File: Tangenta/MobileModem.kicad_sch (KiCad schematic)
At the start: 12 parts, among them J18 1-2199230-5, J19 HYC90-SIM06-180

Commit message: Schematic improvements.
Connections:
- net VPP: no longer names the net of J19.5 (VPP)
- no-connect marks 45 -> 47
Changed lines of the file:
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@@
   (no_connect (at 86.36 123.19))
   (no_connect (at 86.36 113.03))
+  (no_connect (at 39.37 170.18))
   (no_connect (at 60.96 72.39))
   (no_connect (at 151.13 95.25))
   (no_connect (at 60.96 74.93))
   (no_connect (at 60.96 52.07))
+  (no_connect (at 158.75 87.63))
   (no_connect (at 147.32 95.25))
   (no_connect (at 86.36 102.87))
@@
     (stroke (width 0) (type default))
   )
-  (wire (pts (xy 158.75 87.63) (xy 170.18 87.63))
-    (stroke (width 0) (type default))
-  )
   (wire (pts (xy 60.96 100.33) (xy 44.45 100.33))
     (stroke (width 0) (type default))
@@
     (effects (font (size 1.27 1.27)) (justify left bottom))
   )
-  (label "VPP" (at 170.18 87.63 180) (fields_autoplaced)
-    (effects (font (size 1.27 1.27)) (justify right bottom))
-  )
   (label "UIM1_CLK" (at 106.68 90.17 0) (fields_autoplaced)

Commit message: Libraries exported from global to project.
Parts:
- C1: symbol Device:C_Small -> CholaSymbolsPrjLib:C_Small
- H10, H11: symbol Mechanical:MountingHole -> CholaSymbolsPrjLib:MountingHole
- J18: symbol M2_Slot:1-2199230-5 -> CholaSymbolsPrjLib:1-2199230-5
- J19: symbol SIM_Holder:HYC90-SIM06-180 -> CholaSymbolsPrjLib:HYC90-SIM06-180
- R2: symbol Device:R_Small_US -> CholaSymbolsPrjLib:R_Small_US
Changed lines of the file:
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@@
     (effects (font (size 1.27 1.27)) (justify right))
   )
-  (symbol (lib_id "SIM_Holder:HYC90-SIM06-180") (at 148.59 87.63 0) (unit 1)
+  (symbol (lib_id "CholaSymbolsPrjLib:HYC90-SIM06-180") (at 148.59 87.63 0) (unit 1)
     (in_bom yes) (on_board yes) (dnp no) (fields_autoplaced)
     (property "Reference" "J19" (at 148.59 78.74 0)
@@
     )
   )
-  (symbol (lib_id "Mechanical:MountingHole") (at 186.055 76.2 0) (unit 1)
+  (symbol (lib_id "CholaSymbolsPrjLib:MountingHole") (at 186.055 76.2 0) (unit 1)
     (in_bom yes) (on_board yes) (dnp no)
     (property "Reference" "H10" (at 188.595 76.2 0)
@@
     )
   )
-  (symbol (lib_id "Device:C_Small") (at 140.97 68.58 180) (unit 1)
+  (symbol (lib_id "CholaSymbolsPrjLib:C_Small") (at 140.97 68.58 180) (unit 1)
     (in_bom yes) (on_board yes) (dnp no)
     (property "Reference" "C1" (at 137.16 68.58 0)
@@
     )
   )
-  (symbol (lib_id "Device:C_Small") (at 156.21 68.58 180) (unit 1)
+  (symbol (lib_id "CholaSymbolsPrjLib:C_Small") (at 156.21 68.58 180) (unit 1)
     (in_bom yes) (on_board yes) (dnp no)
     (property "Reference" "C1" (at 160.02 68.58 0)
@@
     )
   )
-  (symbol (lib_id "Device:R_Small_US") (at 173.99 74.93 180) (unit 1)
+  (symbol (lib_id "CholaSymbolsPrjLib:R_Small_US") (at 173.99 74.93 180) (unit 1)
     (in_bom yes) (on_board yes) (dnp no)
     (property "Reference" "R2" (at 172.72 74.93 0)
@@
     )
   )
-  (symbol (lib_id "Device:R_Small_US") (at 54.61 77.47 90) (unit 1)
+  (symbol (lib_id "CholaSymbolsPrjLib:R_Small_US") (at 54.61 77.47 90) (unit 1)
     (in_bom yes) (on_board yes) (dnp no)
     (property "Reference" "R2" (at 53.34 76.2 90)
@@
     )
   )
-  (symbol (lib_id "Device:C_Small") (at 124.46 95.25 180) (unit 1)
+  (symbol (lib_id "CholaSymbolsPrjLib:C_Small") (at 124.46 95.25 180) (unit 1)
     (in_bom yes) (on_board yes) (dnp no)
     (property "Reference" "C1" (at 120.65 95.25 0)
@@
     )
   )
-  (symbol (lib_id "Mechanical:MountingHole") (at 186.055 83.82 0) (unit 1)
+  (symbol (lib_id "CholaSymbolsPrjLib:MountingHole") (at 186.055 83.82 0) (unit 1)
     (in_bom yes) (on_board yes) (dnp no)
     (property "Reference" "H11" (at 188.595 83.82 0)
@@
     )
   )
-  (symbol (lib_id "Device:R_Small_US") (at 92.71 57.15 270) (mirror x) (unit 1)
+  (symbol (lib_id "CholaSymbolsPrjLib:R_Small_US") (at 92.71 57.15 270) (mirror x) (unit 1)
     (in_bom yes) (on_board yes) (dnp no)
     (property "Reference" "R2" (at 87.63 55.88 90)
@@
     )
   )
-  (symbol (lib_id "Device:R_Small_US") (at 54.61 128.27 90) (unit 1)
+  (symbol (lib_id "CholaSymbolsPrjLib:R_Small_US") (at 54.61 128.27 90) (unit 1)
     (in_bom yes) (on_board yes) (dnp no)
     (property "Reference" "R2" (at 53.34 127 90)
@@
     )
   )
-  (symbol (lib_id "Device:R_Small_US") (at 124.46 104.14 180) (unit 1)
+  (symbol (lib_id "CholaSymbolsPrjLib:R_Small_US") (at 124.46 104.14 180) (unit 1)
     (in_bom yes) (on_board yes) (dnp no)
     (property "Reference" "R2" (at 123.19 104.14 0)
@@
     )
   )
-  (symbol (lib_id "M2_Slot:1-2199230-5") (at 73.66 44.45 90) (mirror x) (unit 1)
+  (symbol (lib_id "CholaSymbolsPrjLib:1-2199230-5") (at 73.66 44.45 90) (mirror x) (unit 1)
     (in_bom yes) (on_board yes) (dnp no)
     (property "Reference" "J18" (at 66.04 46.99 90)

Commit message: GND ready, before re-annotation.
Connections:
- net CHASSIS: no longer J18.MP1
- no-connect marks 47 -> 48
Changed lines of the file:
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@@
   (no_connect (at 86.36 107.95))
   (no_connect (at 60.96 125.73))
+  (no_connect (at 73.66 44.45))
   (no_connect (at 86.36 82.55))
   (no_connect (at 60.96 97.79))
@@
     (stroke (width 0) (type default))
   )
-  (wire (pts (xy 73.66 41.91) (xy 82.55 41.91))
-    (stroke (width 0) (type default))
-  )
   (wire (pts (xy 86.36 128.27) (xy 102.87 128.27))
     (stroke (width 0) (type default))
@@
     (stroke (width 0) (type default))
   )
-  (wire (pts (xy 73.66 41.91) (xy 73.66 44.45))
-    (stroke (width 0) (type default))
-  )
   (wire (pts (xy 148.59 72.39) (xy 156.21 72.39))
     (stroke (width 0) (type default))
@@
     (effects (font (size 1.27 1.27)) (justify right bottom))
   )
-  (label "CHASSIS" (at 82.55 41.91 180) (fields_autoplaced)
-    (effects (font (size 1.27 1.27)) (justify right bottom))
-  )

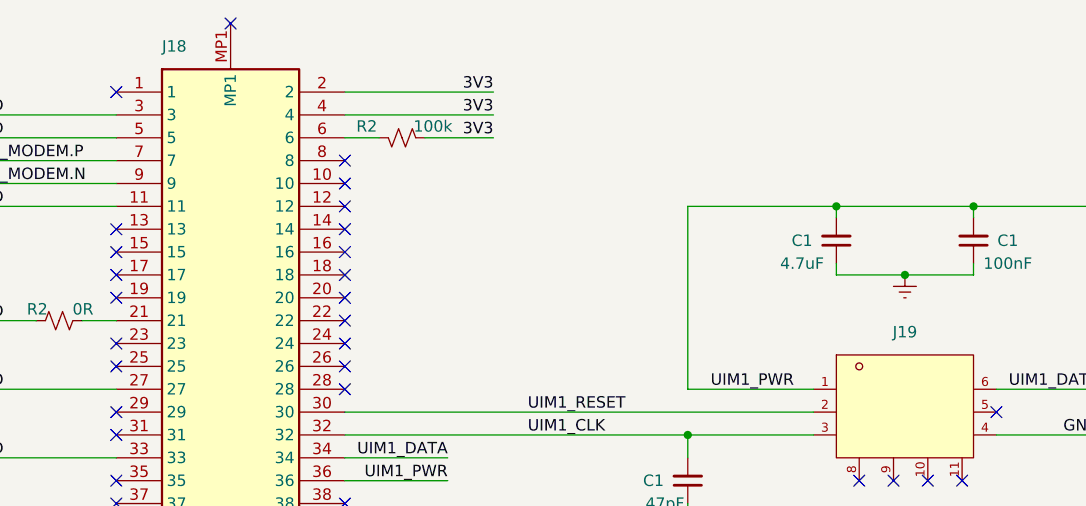
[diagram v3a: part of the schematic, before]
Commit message: Re-annotated. Ready for JLCPCB design verification.
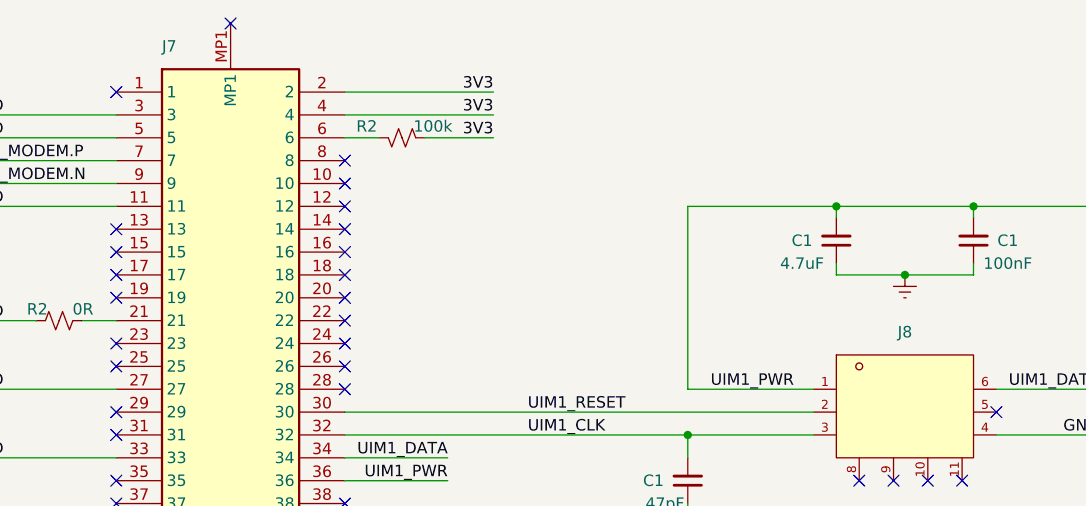
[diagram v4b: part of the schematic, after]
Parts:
- renumbered J18 to J7, J19 to J8
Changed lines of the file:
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@@
   (symbol (lib_id "CholaSymbolsPrjLib:HYC90-SIM06-180") (at 148.59 87.63 0) (unit 1)
     (in_bom yes) (on_board yes) (dnp no) (fields_autoplaced)
-    (property "Reference" "J19" (at 148.59 78.74 0)
+    (property "Reference" "J8" (at 148.59 78.74 0)
       (effects (font (size 1.27 1.27)))
     )
@@
       (project "Tangenta"
         (path "/358d1bcf-7599-4352-8c4d-baa18a5f09e6/f1c5822c-e7b8-40ae-bab0-71fd1c2cfc7c"
-          (reference "J19") (unit 1)
+          (reference "J8") (unit 1)
         )
       )
@@
         )
         (path "/358d1bcf-7599-4352-8c4d-baa18a5f09e6/f1c5822c-e7b8-40ae-bab0-71fd1c2cfc7c"
-          (reference "#PWR045") (unit 1)
+          (reference "#PWR050") (unit 1)
         )
       )
@@
         )
         (path "/358d1bcf-7599-4352-8c4d-baa18a5f09e6/f1c5822c-e7b8-40ae-bab0-71fd1c2cfc7c"
-          (reference "C85") (unit 1)
+          (reference "C71") (unit 1)
         )
       )
@@
         )
         (path "/358d1bcf-7599-4352-8c4d-baa18a5f09e6/f1c5822c-e7b8-40ae-bab0-71fd1c2cfc7c"
-          (reference "C86") (unit 1)
+          (reference "C72") (unit 1)
         )
       )
@@
         )
         (path "/358d1bcf-7599-4352-8c4d-baa18a5f09e6/f1c5822c-e7b8-40ae-bab0-71fd1c2cfc7c"
-          (reference "R52") (unit 1)
+          (reference "R46") (unit 1)
         )
       )
@@
         )
         (path "/358d1bcf-7599-4352-8c4d-baa18a5f09e6/f1c5822c-e7b8-40ae-bab0-71fd1c2cfc7c"
-          (reference "#PWR046") (unit 1)
+          (reference "#PWR051") (unit 1)
         )
       )
@@
         )
         (path "/358d1bcf-7599-4352-8c4d-baa18a5f09e6/f1c5822c-e7b8-40ae-bab0-71fd1c2cfc7c"
-          (reference "R48") (unit 1)
+          (reference "R42") (unit 1)
         )
       )
@@
         )
         (path "/358d1bcf-7599-4352-8c4d-baa18a5f09e6/f1c5822c-e7b8-40ae-bab0-71fd1c2cfc7c"
-          (reference "C84") (unit 1)
+          (reference "C70") (unit 1)
         )
       )
@@
         )
         (path "/358d1bcf-7599-4352-8c4d-baa18a5f09e6/f1c5822c-e7b8-40ae-bab0-71fd1c2cfc7c"
-          (reference "R50") (unit 1)
+          (reference "R44") (unit 1)
         )
       )
@@
         )
         (path "/358d1bcf-7599-4352-8c4d-baa18a5f09e6/f1c5822c-e7b8-40ae-bab0-71fd1c2cfc7c"
-          (reference "R49") (unit 1)
+          (reference "R43") (unit 1)
         )
       )
@@
         )
         (path "/358d1bcf-7599-4352-8c4d-baa18a5f09e6/f1c5822c-e7b8-40ae-bab0-71fd1c2cfc7c"
-          (reference "#PWR035") (unit 1)
+          (reference "#PWR049") (unit 1)
         )
       )
@@
         )
         (path "/358d1bcf-7599-4352-8c4d-baa18a5f09e6/f1c5822c-e7b8-40ae-bab0-71fd1c2cfc7c"
-          (reference "R51") (unit 1)
+          (reference "R45") (unit 1)
         )
       )
@@
   (symbol (lib_id "CholaSymbolsPrjLib:1-2199230-5") (at 73.66 44.45 90) (mirror x) (unit 1)
     (in_bom yes) (on_board yes) (dnp no)
-    (property "Reference" "J18" (at 66.04 46.99 90)
+    (property "Reference" "J7" (at 66.04 46.99 90)
       (effects (font (size 1.27 1.27)) (justify right))
     )
@@
       (project "Tangenta"
         (path "/358d1bcf-7599-4352-8c4d-baa18a5f09e6/f1c5822c-e7b8-40ae-bab0-71fd1c2cfc7c"
-          (reference "J18") (unit 1)
-        )
-      )
+          (reference "J7") (unit 1)
+        )
+      )

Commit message: initialize branch
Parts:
- renumbered C1 to C70, C1 to C71, C1 to C72, R2 to R42, R2 to R43, R2 to R44, R2 to R45, R2 to R46
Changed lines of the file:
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@@
   (symbol (lib_id "power:GNDREF") (at 124.46 111.76 0) (unit 1)
     (in_bom yes) (on_board yes) (dnp no) (fields_autoplaced)
-    (property "Reference" "#PWR030" (at 124.46 118.11 0)
+    (property "Reference" "#PWR050" (at 124.46 118.11 0)
       (effects (font (size 1.27 1.27)) hide)
     )
@@
     (instances
       (project "Tangenta"
-        (path "/358d1bcf-7599-4352-8c4d-baa18a5f09e6/b1871a4d-6a35-44e2-a9a2-9a4af684371d"
-          (reference "#PWR030") (unit 1)
-        )
         (path "/358d1bcf-7599-4352-8c4d-baa18a5f09e6/f1c5822c-e7b8-40ae-bab0-71fd1c2cfc7c"
           (reference "#PWR050") (unit 1)
@@
   (symbol (lib_id "CholaSymbolsPrjLib:C_Small") (at 140.97 68.58 180) (unit 1)
     (in_bom yes) (on_board yes) (dnp no)
-    (property "Reference" "C1" (at 137.16 68.58 0)
+    (property "Reference" "C71" (at 137.16 68.58 0)
       (effects (font (size 1.27 1.27)))
     )
@@
     (instances
       (project "Tangenta"
-        (path "/358d1bcf-7599-4352-8c4d-baa18a5f09e6/8215796b-9611-4f43-bcc5-319f8414b8a6"
-          (reference "C1") (unit 1)
-        )
-        (path "/358d1bcf-7599-4352-8c4d-baa18a5f09e6/d6c05402-162e-441f-bed8-be7996260fb4"
-          (reference "C9") (unit 1)
-        )
-        (path "/358d1bcf-7599-4352-8c4d-baa18a5f09e6/b1871a4d-6a35-44e2-a9a2-9a4af684371d"
-          (reference "C35") (unit 1)
-        )
         (path "/358d1bcf-7599-4352-8c4d-baa18a5f09e6/f1c5822c-e7b8-40ae-bab0-71fd1c2cfc7c"
           (reference "C71") (unit 1)
@@
   (symbol (lib_id "CholaSymbolsPrjLib:C_Small") (at 156.21 68.58 180) (unit 1)
     (in_bom yes) (on_board yes) (dnp no)
-    (property "Reference" "C1" (at 160.02 68.58 0)
+    (property "Reference" "C72" (at 160.02 68.58 0)
       (effects (font (size 1.27 1.27)))
     )
@@
     (instances
       (project "Tangenta"
-        (path "/358d1bcf-7599-4352-8c4d-baa18a5f09e6/8215796b-9611-4f43-bcc5-319f8414b8a6"
-          (reference "C1") (unit 1)
-        )
-        (path "/358d1bcf-7599-4352-8c4d-baa18a5f09e6/d6c05402-162e-441f-bed8-be7996260fb4"
-          (reference "C9") (unit 1)
-        )
-        (path "/358d1bcf-7599-4352-8c4d-baa18a5f09e6/b1871a4d-6a35-44e2-a9a2-9a4af684371d"
-          (reference "C35") (unit 1)
-        )
         (path "/358d1bcf-7599-4352-8c4d-baa18a5f09e6/f1c5822c-e7b8-40ae-bab0-71fd1c2cfc7c"
           (reference "C72") (unit 1)
@@
   (symbol (lib_id "CholaSymbolsPrjLib:R_Small_US") (at 173.99 74.93 180) (unit 1)
     (in_bom yes) (on_board yes) (dnp no)
-    (property "Reference" "R2" (at 172.72 74.93 0)
+    (property "Reference" "R46" (at 172.72 74.93 0)
       (effects (font (size 1.27 1.27)) (justify left))
     )
@@
     (instances
       (project "Tangenta"
-        (path "/358d1bcf-7599-4352-8c4d-baa18a5f09e6/8215796b-9611-4f43-bcc5-319f8414b8a6"
-          (reference "R2") (unit 1)
-        )
-        (path "/358d1bcf-7599-4352-8c4d-baa18a5f09e6/d6c05402-162e-441f-bed8-be7996260fb4"
-          (reference "R18") (unit 1)
-        )
-        (path "/358d1bcf-7599-4352-8c4d-baa18a5f09e6/b1871a4d-6a35-44e2-a9a2-9a4af684371d"
-          (reference "R26") (unit 1)
-        )
         (path "/358d1bcf-7599-4352-8c4d-baa18a5f09e6/f1c5822c-e7b8-40ae-bab0-71fd1c2cfc7c"
           (reference "R46") (unit 1)
@@
   (symbol (lib_id "power:GNDREF") (at 148.59 72.39 0) (unit 1)
     (in_bom yes) (on_board yes) (dnp no) (fields_autoplaced)
-    (property "Reference" "#PWR030" (at 148.59 78.74 0)
+    (property "Reference" "#PWR051" (at 148.59 78.74 0)
       (effects (font (size 1.27 1.27)) hide)
     )
@@
     (instances
       (project "Tangenta"
-        (path "/358d1bcf-7599-4352-8c4d-baa18a5f09e6/b1871a4d-6a35-44e2-a9a2-9a4af684371d"
-          (reference "#PWR030") (unit 1)
-        )
         (path "/358d1bcf-7599-4352-8c4d-baa18a5f09e6/f1c5822c-e7b8-40ae-bab0-71fd1c2cfc7c"
           (reference "#PWR051") (unit 1)
@@
   (symbol (lib_id "CholaSymbolsPrjLib:R_Small_US") (at 54.61 77.47 90) (unit 1)
     (in_bom yes) (on_board yes) (dnp no)
-    (property "Reference" "R2" (at 53.34 76.2 90)
+    (property "Reference" "R42" (at 53.34 76.2 90)
       (effects (font (size 1.27 1.27)) (justify left))
     )
@@
     (instances
       (project "Tangenta"
-        (path "/358d1bcf-7599-4352-8c4d-baa18a5f09e6/8215796b-9611-4f43-bcc5-319f8414b8a6"
-          (reference "R2") (unit 1)
-        )
-        (path "/358d1bcf-7599-4352-8c4d-baa18a5f09e6/d6c05402-162e-441f-bed8-be7996260fb4"
-          (reference "R18") (unit 1)
-        )
-        (path "/358d1bcf-7599-4352-8c4d-baa18a5f09e6/b1871a4d-6a35-44e2-a9a2-9a4af684371d"
-          (reference "R26") (unit 1)
-        )
-        (path "/358d1bcf-7599-4352-8c4d-baa18a5f09e6/6a8c68b5-4a7d-449e-86f6-34ced6d1cb55"
-          (reference "R45") (unit 1)
-        )
         (path "/358d1bcf-7599-4352-8c4d-baa18a5f09e6/f1c5822c-e7b8-40ae-bab0-71fd1c2cfc7c"
           (reference "R42") (unit 1)
@@
   (symbol (lib_id "CholaSymbolsPrjLib:C_Small") (at 124.46 95.25 180) (unit 1)
     (in_bom yes) (on_board yes) (dnp no)
-    (property "Reference" "C1" (at 120.65 95.25 0)
+    (property "Reference" "C70" (at 120.65 95.25 0)
       (effects (font (size 1.27 1.27)))
     )
@@
     (instances
       (project "Tangenta"
-        (path "/358d1bcf-7599-4352-8c4d-baa18a5f09e6/8215796b-9611-4f43-bcc5-319f8414b8a6"
-          (reference "C1") (unit 1)
-        )
-        (path "/358d1bcf-7599-4352-8c4d-baa18a5f09e6/d6c05402-162e-441f-bed8-be7996260fb4"
-          (reference "C9") (unit 1)
-        )
-        (path "/358d1bcf-7599-4352-8c4d-baa18a5f09e6/b1871a4d-6a35-44e2-a9a2-9a4af684371d"
-          (reference "C35") (unit 1)
-        )
         (path "/358d1bcf-7599-4352-8c4d-baa18a5f09e6/f1c5822c-e7b8-40ae-bab0-71fd1c2cfc7c"
           (reference "C70") (unit 1)
@@
   (symbol (lib_id "CholaSymbolsPrjLib:R_Small_US") (at 92.71 57.15 270) (mirror x) (unit 1)
     (in_bom yes) (on_board yes) (dnp no)
-    (property "Reference" "R2" (at 87.63 55.88 90)
+    (property "Reference" "R44" (at 87.63 55.88 90)
       (effects (font (size 1.27 1.27)) (justify left))
     )
@@
     (instances
       (project "Tangenta"
-        (path "/358d1bcf-7599-4352-8c4d-baa18a5f09e6/8215796b-9611-4f43-bcc5-319f8414b8a6"
-          (reference "R2") (unit 1)
-        )
-        (path "/358d1bcf-7599-4352-8c4d-baa18a5f09e6/d6c05402-162e-441f-bed8-be7996260fb4"
-          (reference "R18") (unit 1)
-        )
-        (path "/358d1bcf-7599-4352-8c4d-baa18a5f09e6/b1871a4d-6a35-44e2-a9a2-9a4af684371d"
-          (reference "R26") (unit 1)
-        )
-        (path "/358d1bcf-7599-4352-8c4d-baa18a5f09e6/6a8c68b5-4a7d-449e-86f6-34ced6d1cb55"
-          (reference "R45") (unit 1)
-        )
         (path "/358d1bcf-7599-4352-8c4d-baa18a5f09e6/f1c5822c-e7b8-40ae-bab0-71fd1c2cfc7c"
           (reference "R44") (unit 1)
@@
   (symbol (lib_id "CholaSymbolsPrjLib:R_Small_US") (at 54.61 128.27 90) (unit 1)
     (in_bom yes) (on_board yes) (dnp no)
-    (property "Reference" "R2" (at 53.34 127 90)
+    (property "Reference" "R43" (at 53.34 127 90)
       (effects (font (size 1.27 1.27)) (justify left))
     )
@@
     (instances
       (project "Tangenta"
-        (path "/358d1bcf-7599-4352-8c4d-baa18a5f09e6/8215796b-9611-4f43-bcc5-319f8414b8a6"
-          (reference "R2") (unit 1)
-        )
-        (path "/358d1bcf-7599-4352-8c4d-baa18a5f09e6/d6c05402-162e-441f-bed8-be7996260fb4"
-          (reference "R18") (unit 1)
-        )
-        (path "/358d1bcf-7599-4352-8c4d-baa18a5f09e6/b1871a4d-6a35-44e2-a9a2-9a4af684371d"
-          (reference "R26") (unit 1)
-        )
-        (path "/358d1bcf-7599-4352-8c4d-baa18a5f09e6/6a8c68b5-4a7d-449e-86f6-34ced6d1cb55"
-          (reference "R45") (unit 1)
-        )
         (path "/358d1bcf-7599-4352-8c4d-baa18a5f09e6/f1c5822c-e7b8-40ae-bab0-71fd1c2cfc7c"
           (reference "R43") (unit 1)
@@
   (symbol (lib_id "power:GNDREF") (at 39.37 166.37 90) (unit 1)
     (in_bom yes) (on_board yes) (dnp no) (fields_autoplaced)
-    (property "Reference" "#PWR030" (at 45.72 166.37 0)
+    (property "Reference" "#PWR049" (at 45.72 166.37 0)
       (effects (font (size 1.27 1.27)) hide)
     )
@@
     (instances
       (project "Tangenta"
-        (path "/358d1bcf-7599-4352-8c4d-baa18a5f09e6/b1871a4d-6a35-44e2-a9a2-9a4af684371d"
-          (reference "#PWR030") (unit 1)
-        )
         (path "/358d1bcf-7599-4352-8c4d-baa18a5f09e6/f1c5822c-e7b8-40ae-bab0-71fd1c2cfc7c"
           (reference "#PWR049") (unit 1)
@@
   (symbol (lib_id "CholaSymbolsPrjLib:R_Small_US") (at 124.46 104.14 180) (unit 1)
     (in_bom yes) (on_board yes) (dnp no)
-    (property "Reference" "R2" (at 123.19 104.14 0)
+    (property "Reference" "R45" (at 123.19 104.14 0)
       (effects (font (size 1.27 1.27)) (justify left))
     )
@@
     (instances
       (project "Tangenta"
-        (path "/358d1bcf-7599-4352-8c4d-baa18a5f09e6/8215796b-9611-4f43-bcc5-319f8414b8a6"
-          (reference "R2") (unit 1)
-        )
-        (path "/358d1bcf-7599-4352-8c4d-baa18a5f09e6/d6c05402-162e-441f-bed8-be7996260fb4"
-          (reference "R18") (unit 1)
-        )
-        (path "/358d1bcf-7599-4352-8c4d-baa18a5f09e6/b1871a4d-6a35-44e2-a9a2-9a4af684371d"
-          (reference "R26") (unit 1)
-        )
         (path "/358d1bcf-7599-4352-8c4d-baa18a5f09e6/f1c5822c-e7b8-40ae-bab0-71fd1c2cfc7c"
           (reference "R45") (unit 1)

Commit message: J6-J8,J22-J25,S1,U21
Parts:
- J7: footprint M2_Slot:M2_Slot -> CholaFootprintsPrjLib:M2_Slot
- J8: footprint SIM_Holder:SIM-SMD_HYC90-SIM06-180 -> CholaFootprintsPrjLib:SIM-SMD_HYC90-SIM06-180
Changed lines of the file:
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@@
       (effects (font (size 1.27 1.27)) hide)
     )
-    (property "Footprint" "SIM_Holder:SIM-SMD_HYC90-SIM06-180" (at 149.86 80.01 0)
+    (property "Footprint" "CholaFootprintsPrjLib:SIM-SMD_HYC90-SIM06-180" (at 149.86 80.01 0)
       (effects (font (size 1.27 1.27)) hide)
     )
@@
       (effects (font (size 1.27 1.27)) (justify right))
     )
-    (property "Footprint" "M2_Slot:M2_Slot" (at 163.5 139.7 0)
+    (property "Footprint" "CholaFootprintsPrjLib:M2_Slot" (at 163.5 139.7 0)
       (effects (font (size 1.27 1.27)) (justify left top) hide)
     )
